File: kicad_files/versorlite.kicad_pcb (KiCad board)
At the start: 4 copper layers, 33 x 81.3 mm, 131 parts, among them J1 Conn_01x01_Socket, J3 RFD900ux 10 Pin Header, J4 Conn_ARM_JTAG_SWD_10, J5 RFD900ux 3 Pin Power Select, J6 USB_C_Receptacle_USB2.0_16P, J7 Micro_SD_Card_Det2, J8 Conn_01x02_Socket, J9 IGN_1, Q1 FDMC510P-MS, Q3 AO3400A, SW1 SW_Push, SW2 SW_Push, U1 STM32F407VGTx, U10 W25Q128JVS, U11 LT1963AxST-3.3, U12 AP63205WU, U13 74LVC1G125, U2 MS5611-01BA, U3 BMI088, U4 MMC5983MA, U5 MAX-M10S, U6 BMP388, U7 LSM6DSM, U9 WE-TVS-82400102, Y1 LFXTAL036869Reel 8MHz Crystal

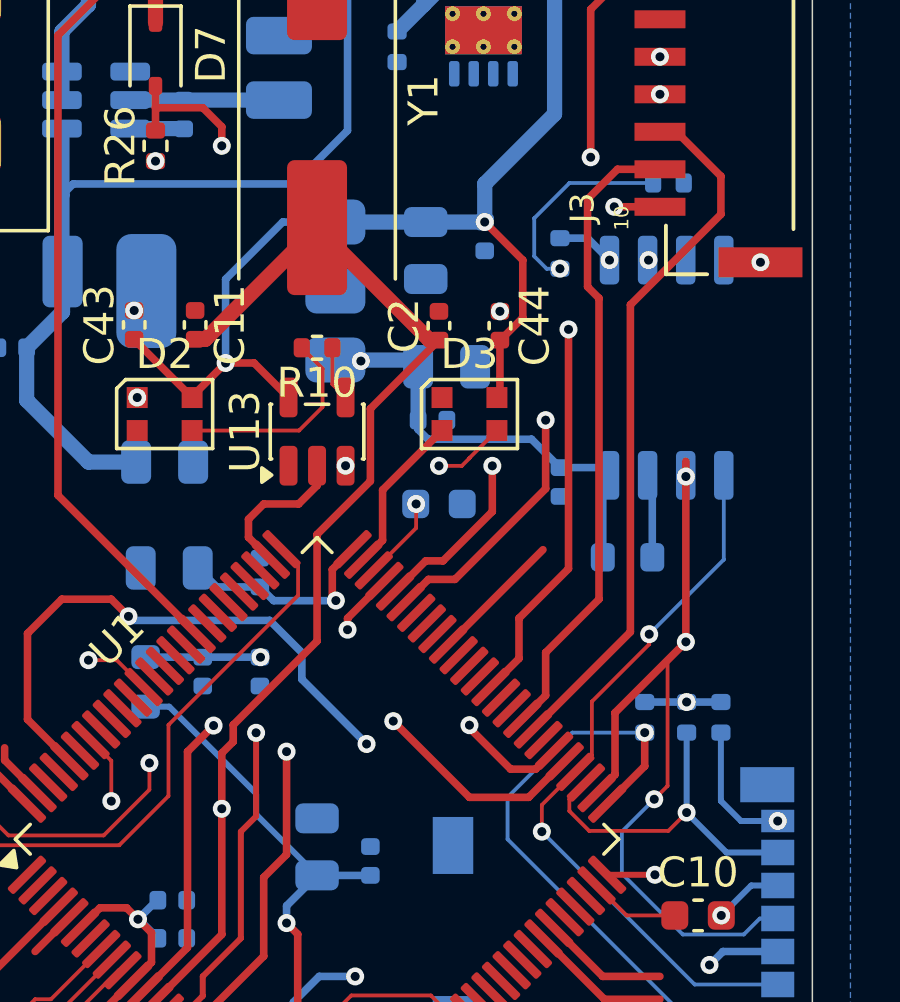
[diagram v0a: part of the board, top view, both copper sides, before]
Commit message: oop missed two traces
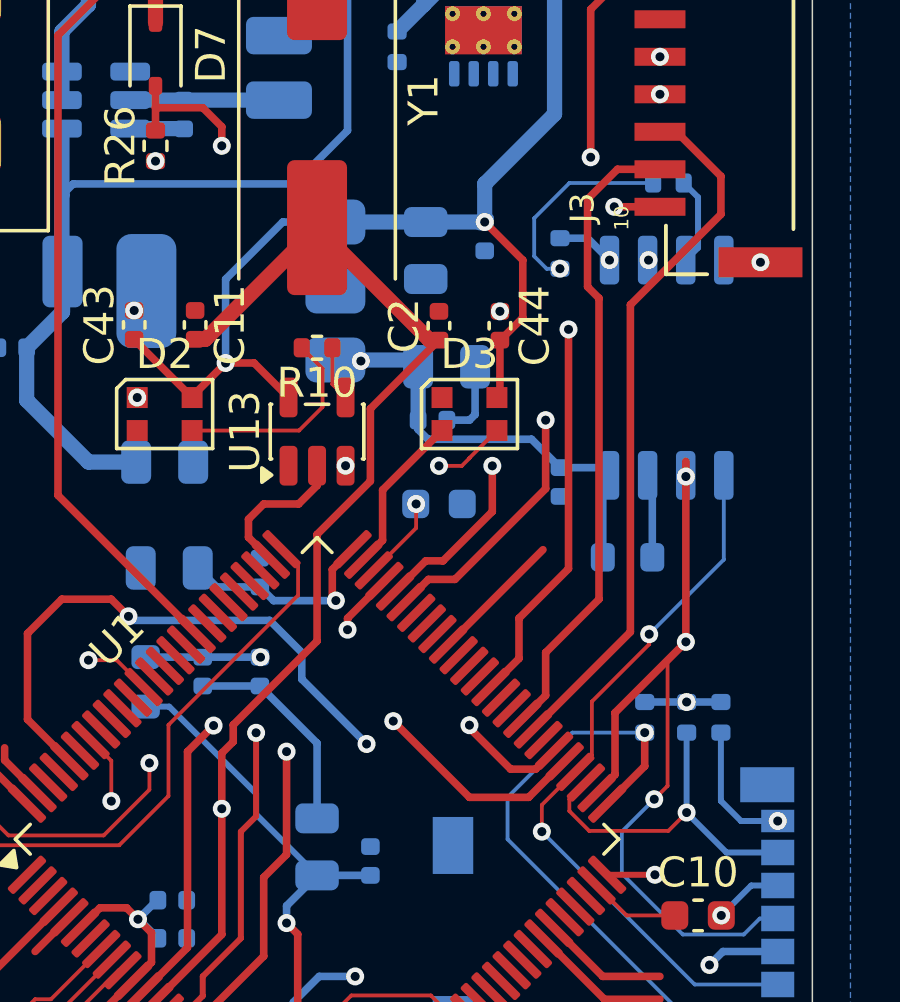
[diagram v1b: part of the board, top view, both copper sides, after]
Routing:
- net GND: track 95.2 -> 104.9 mm
- net Net-(U10-~{WP}/IO_{2}): track 0.00 -> 2.94 mm
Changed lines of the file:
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@@
 	)
 	(segment
+		(start 147.838001 95.758)
+		(end 148.59 95.758)
+		(width 0.254)
+		(layer "B.Cu")
+		(net "GND")
+	)
+	(segment
 		(start 143.6135 120.904)
 		(end 143.925999 120.904)
@@
 	)
 	(segment
+		(start 141.605 104.62)
+		(end 139.7 104.62)
+		(width 0.254)
+		(layer "B.Cu")
+		(net "GND")
+	)
+	(segment
 		(start 143.891 117.475)
 		(end 143.256 116.84)
@@
 	)
 	(segment
+		(start 141.605 104.62)
+		(end 143.51 106.525)
+		(width 0.254)
+		(layer "B.Cu")
+		(net "GND")
+	)
+	(segment
 		(start 140.137 121.849)
 		(end 140.462 122.174)
@@
 	)
 	(segment
+		(start 143.51 106.525)
+		(end 143.51 109.032001)
+		(width 0.254)
+		(layer "B.Cu")
+		(net "GND")
+	)
+	(segment
 		(start 130.302 121.412)
 		(end 130.301999 122.682001)
@@
 	)
 	(segment
+		(start 148.777999 95.570001)
+		(end 148.777999 93.98)
+		(width 0.254)
+		(layer "B.Cu")
+		(net "GND")
+	)
+	(segment
 		(start 141.732 122.174)
 		(end 143.004001 120.901999)
@@
 	)
 	(segment
+		(start 148.59 95.758)
+		(end 148.777999 95.570001)
+		(width 0.254)
+		(layer "B.Cu")
+		(net "GND")
+	)
+	(segment
 		(start 143.256 115.951)
 		(end 143.581 115.626)
@@
 	)
 	(segment
-		(start 143.002 79.502)
-		(end 142.494 80.01)
-		(width 0.254)
-		(layer "B.Cu")
-		(net "Net-(D8-K)")
-	)
-	(segment
-		(start 135.89 81.915)
-		(end 135.89 80.01)
-		(width 0.508)
-		(layer "B.Cu")
-		(net "Net-(D8-K)")
-	)
-	(segment
-		(start 135.0065 84.140001)
-		(end 135.0065 85.09)
-		(width 0.508)
-		(layer "B.Cu")
-		(net "Net-(D8-K)")
-	)
-	(segment
-		(start 139.954 80.01)
-		(end 141.732 80.01)
-		(width 0.508)
-		(layer "B.Cu")
-		(net "Net-(D8-K)")
-	)
-	(segment
-		(start 142.494 80.01)
-		(end 141.732 80.01)
-		(width 0.254)
-		(layer "B.Cu")
-		(net "Net-(D8-K)")
-	)
-	(segment
-		(start 135.0065 82.7985)
-		(end 135.89 81.915)
-		(width 0.508)
-		(layer "B.Cu")
-		(net "Net-(D8-K)")
-	)
-	(segment
-		(start 135.0065 84.140001)
-		(end 135.0065 82.7985)
-		(width 0.508)
-		(layer "B.Cu")
-		(net "Net-(D8-K)")
-	)
-	(segment
-		(start 143.002 75.692)
-		(end 143.002 79.502)
-		(width 0.254)
-		(layer "B.Cu")
-		(net "Net-(D8-K)")
-	)
-	(segment
-		(start 135.89 80.01)
-		(end 139.954 80.01)
-		(width 0.508)
-		(layer "B.Cu")
-		(net "Net-(D8-K)")
-	)
-	(segment
 		(start 144.526 81.28)
 		(end 144.526 86.106)
@@
 	)
 	(segment
+		(start 143.002 79.502)
+		(end 142.494 80.01)
+		(width 0.254)
+		(layer "B.Cu")
+		(net "Net-(D8-K)")
+	)
+	(segment
+		(start 135.89 81.915)
+		(end 135.89 80.01)
+		(width 0.508)
+		(layer "B.Cu")
+		(net "Net-(D8-K)")
+	)
+	(segment
+		(start 135.0065 84.140001)
+		(end 135.0065 85.09)
+		(width 0.508)
+		(layer "B.Cu")
+		(net "Net-(D8-K)")
+	)
+	(segment
+		(start 139.954 80.01)
+		(end 141.732 80.01)
+		(width 0.508)
+		(layer "B.Cu")
+		(net "Net-(D8-K)")
+	)
+	(segment
+		(start 142.494 80.01)
+		(end 141.732 80.01)
+		(width 0.254)
+		(layer "B.Cu")
+		(net "Net-(D8-K)")
+	)
+	(segment
+		(start 135.0065 82.7985)
+		(end 135.89 81.915)
+		(width 0.508)
+		(layer "B.Cu")
+		(net "Net-(D8-K)")
+	)
+	(segment
+		(start 135.0065 84.140001)
+		(end 135.0065 82.7985)
+		(width 0.508)
+		(layer "B.Cu")
+		(net "Net-(D8-K)")
+	)
+	(segment
+		(start 143.002 75.692)
+		(end 143.002 79.502)
+		(width 0.254)
+		(layer "B.Cu")
+		(net "Net-(D8-K)")
+	)
+	(segment
+		(start 135.89 80.01)
+		(end 139.954 80.01)
+		(width 0.508)
+		(layer "B.Cu")
+		(net "Net-(D8-K)")
+	)
+	(segment
 		(start 133.1575 131.8645)
 		(end 133.1575 129.3195)
@@
 	)
 	(segment
+		(start 156.21 90.0115)
+		(end 156.21 88.330369)
+		(width 0.2)
+		(layer "B.Cu")
+		(net "Net-(U10-~{WP}{slash}IO_{2})")
+	)
+	(segment
+		(start 155.798185 90.423315)
+		(end 156.21 90.0115)
+		(width 0.2)
+		(layer "B.Cu")
+		(net "Net-(U10-~{WP}{slash}IO_{2})")
+	)
+	(segment
+		(start 156.21 88.330369)
+		(end 155.732816 87.853185)
+		(width 0.2)
+		(layer "B.Cu")
+		(net "Net-(U10-~{WP}{slash}IO_{2})")
+	)
+	(segment

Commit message: Quick edits, authors
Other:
- board text added: "Apr '26"
- board text added: "Charley Z"
- board text added: "Claire J"
- board text added: "Kai B"
- board text added: "Nancy C"
- board text added: "Olivia K"
- board text added: "Versor Lite v0.1"
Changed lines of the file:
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@@
 		(tags "resistor")
 		(property "Reference" "R8"
-			(at 0 1.43 0)
+			(at 0 -1.27 0)
 			(layer "B.SilkS")
 			(effects
@@
 		(layer "Edge.Cuts")
 	)
+	(gr_text "Olivia K"
+		(at 138.43 139.446 0)
+		(layer "B.SilkS")
+		(effects
+			(font
+				(size 0.5 0.5)
+				(thickness 0.1)
+				(bold yes)
+			)
+			(justify left bottom mirror)
+		)
+	)
+	(gr_text "Claire J"
+		(at 138.43 140.462 0)
+		(layer "B.SilkS")
+		(effects
+			(font
+				(size 0.5 0.5)
+				(thickness 0.1)
+				(bold yes)
+			)
+			(justify left bottom mirror)
+		)
+	)
+	(gr_text "Apr '26"
+		(at 138.43 141.478 0)
+		(layer "B.SilkS")
+		(effects
+			(font
+				(size 0.5 0.5)
+				(thickness 0.1)
+				(bold yes)
+			)
+			(justify left bottom mirror)
+		)
+	)
+	(gr_text "Versor Lite v0.1"
+		(at 146.558 140.97 0)
+		(layer "B.SilkS")
+		(effects
+			(font
+				(size 0.5 0.5)
+				(thickness 0.1)
+				(bold yes)
+			)
+			(justify left bottom mirror)
+		)
+	)
+	(gr_text "Kai B"
+		(at 151.638 140.462 0)
+		(layer "B.SilkS")
+		(effects
+			(font
+				(size 0.5 0.5)
+				(thickness 0.1)
+				(bold yes)
+			)
+			(justify left bottom mirror)
+		)
+	)
+	(gr_text "Charley Z"
+		(at 152.4 139.192 0)
+		(layer "B.SilkS")
+		(effects
+			(font
+				(size 0.5 0.5)
+				(thickness 0.1)
+				(bold yes)
+			)
+			(justify left bottom mirror)
+		)
+	)
+	(gr_text "Nancy C"
+		(at 152.4 141.605 0)
+		(layer "B.SilkS")
+		(effects
+			(font
+				(size 0.5 0.5)
+				(thickness 0.1)
+				(bold yes)
+			)
+			(justify left bottom mirror)
+		)
+	)
 	(via

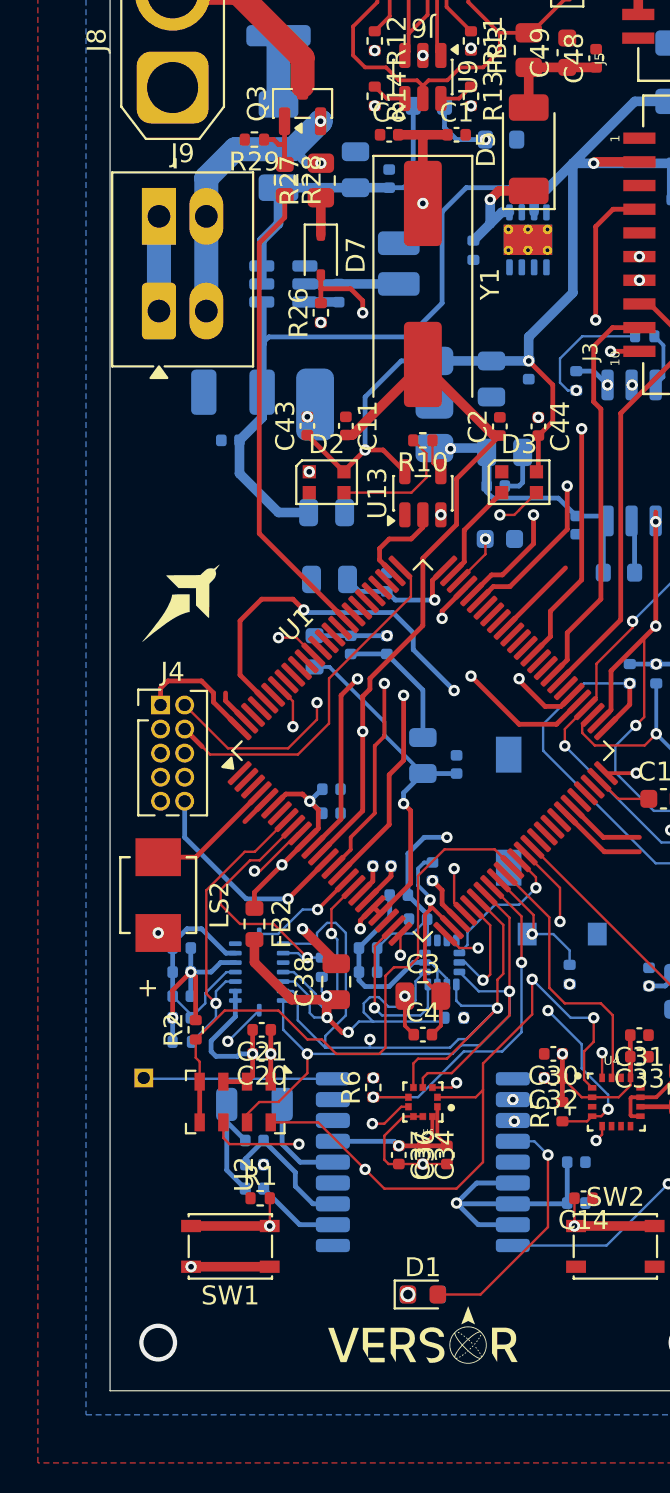
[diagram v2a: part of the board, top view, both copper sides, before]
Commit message: Add second pyro channel
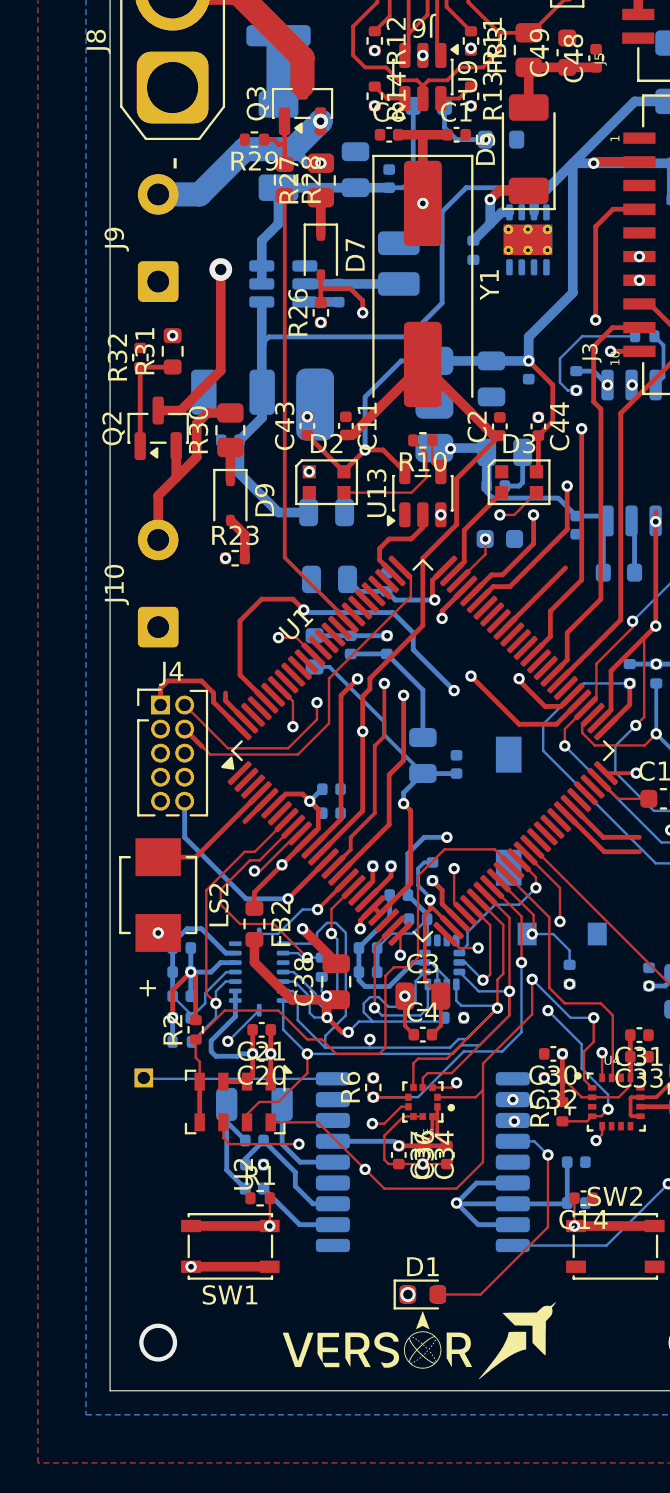
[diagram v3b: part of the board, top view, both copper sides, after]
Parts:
- added D9: CUS10S30,H3F, Diode_SMD:D_SOD-323, F.Cu at (133.3, 96.5)
- added J10: IGN_2, Connector_Wire:SolderWire-0.5sqmm_1x02_P4.6mm_D0.9mm_OD2.1mm, F.Cu at (129.5, 103.2)
- added Q2: AO3400A, Package_TO_SOT_SMD:SOT-23, F.Cu at (129.5, 92.7)
- added R23: 10kΩ, Resistor_SMD:R_0402_1005Metric, F.Cu at (133.6, 99.6)
- added R30: 1kΩ, Resistor_SMD:R_0805_2012Metric, F.Cu at (133.3, 92.8)
- added R31: 100Ω, Resistor_SMD:R_0603_1608Metric, F.Cu at (130.3, 88.6)
- added R32: 10kΩ, Resistor_SMD:R_0402_1005Metric, F.Cu at (128.6, 89.0)
- J9: footprint TerminalBlock_Phoenix:TerminalBlock_Phoenix_PTSM-0,5-2-2.5-H-THR_1x02_P2.50mm_Horizontal -> Connector_Wire:SolderWire-0.5sqmm_1x02_P4.6mm_D0.9mm_OD2.1mm
- moved G*** 42.8 mm to (148.6, 140.8)
- moved G*** 2.41 mm to (141.1, 141.2)
- moved J9 1.56 mm to (129.5, 85.0), turned to 90 degrees
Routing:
- net +9V: track 9.75 -> 36.2 mm, vias 0 -> 1
- net Net-(J10-Pin_2): track 0.00 -> 10.7 mm
- net Net-(Q2-G): track 0.00 -> 5.87 mm
- net GND: track 104.9 -> 99.9 mm
- net Net-(J9-Pin_2): track 16.1 -> 12.0 mm
- net Net-(D9-A): track 0.00 -> 2.31 mm
- net +3.3V_MAIN: track 109.3 -> 111.6 mm, vias 14 -> 15
- net Net-(D9-K): track 0.00 -> 1.75 mm
- net /MCU/IGN_SIG: track 24.9 -> 24.3 mm
- net unconnected-(R31-Pad2): vias 0 -> 1

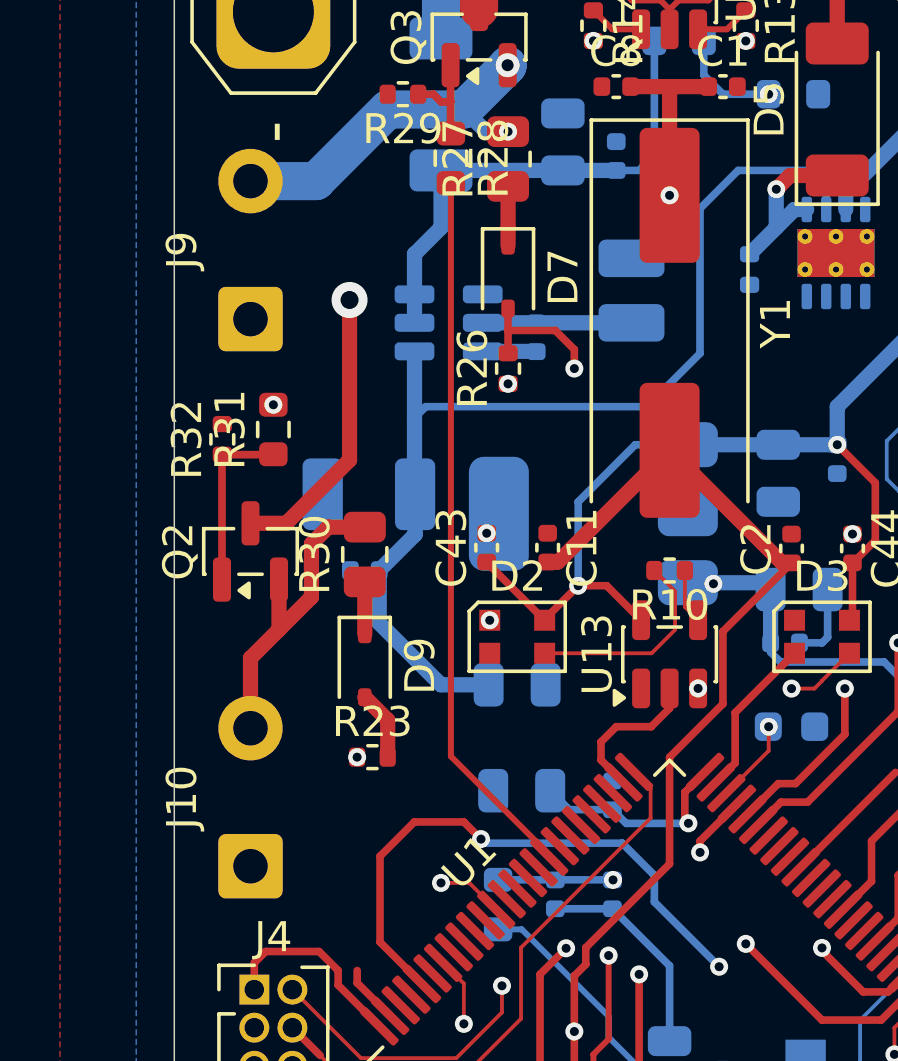
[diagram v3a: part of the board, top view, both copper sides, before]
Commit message: Connect IGN2 signal, rearrange
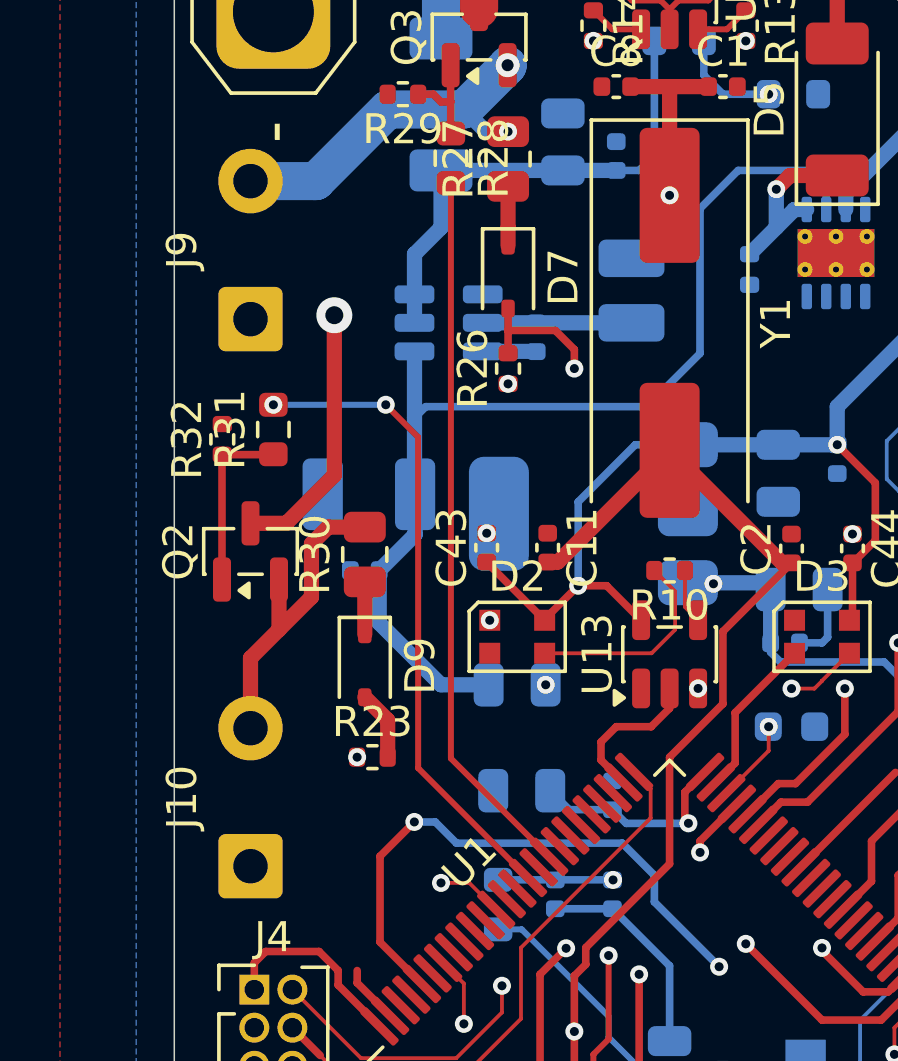
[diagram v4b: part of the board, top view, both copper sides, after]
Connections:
- R31 pad 2: unconnected-(R31-Pad2) -> /MCU/IGN2_SIG
- U1 pad 86: unconnected-(U1-PD5-Pad86) -> /MCU/IGN2_SIG
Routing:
- net /MCU/IGN2_SIG: track 0.00 -> 21.5 mm, vias 0 -> 2
- net unconnected-(R31-Pad2): vias 1 -> 0
- net GND: vias 21 -> 22
